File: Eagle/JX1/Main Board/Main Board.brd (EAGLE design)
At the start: 95.2 x 67.3 mm, 16 parts, among them U1 SN74HC595N, U2 SN74HC595N

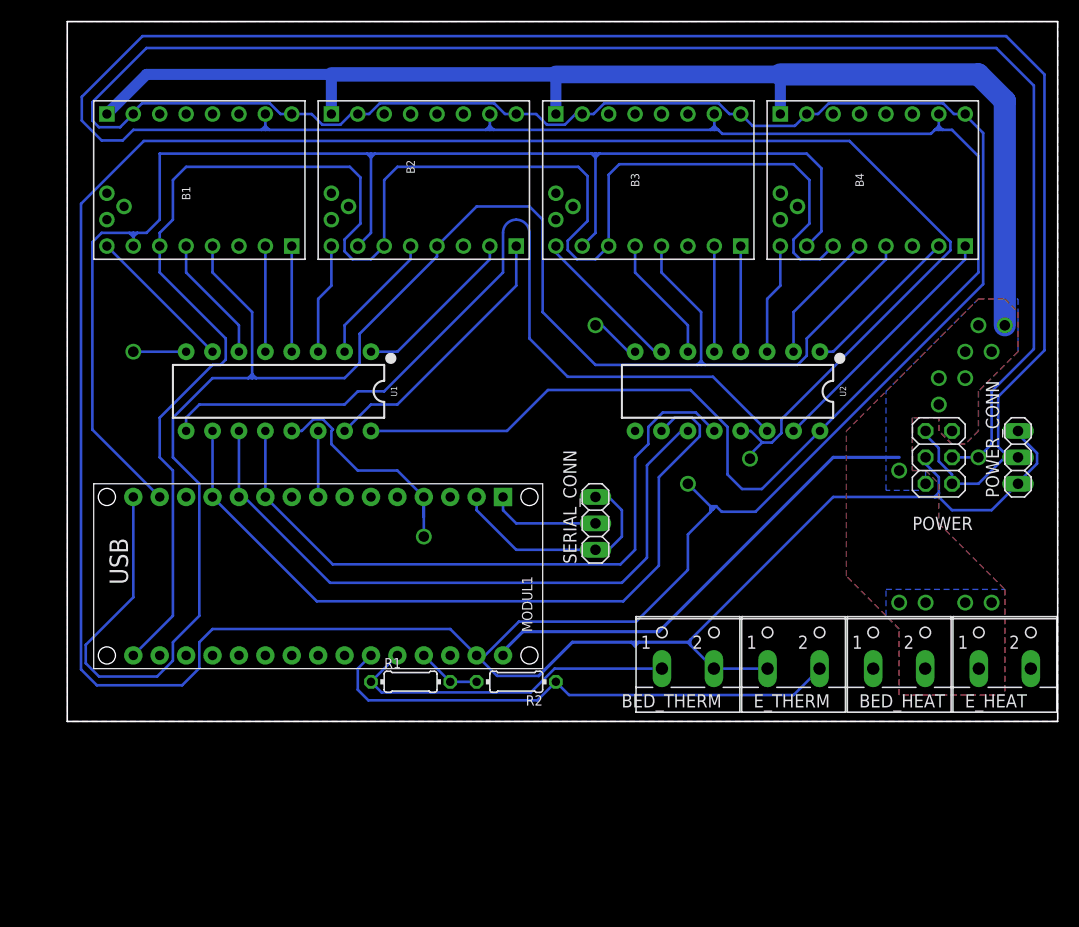
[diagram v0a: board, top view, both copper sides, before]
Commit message: Started added power mosfets for heaters
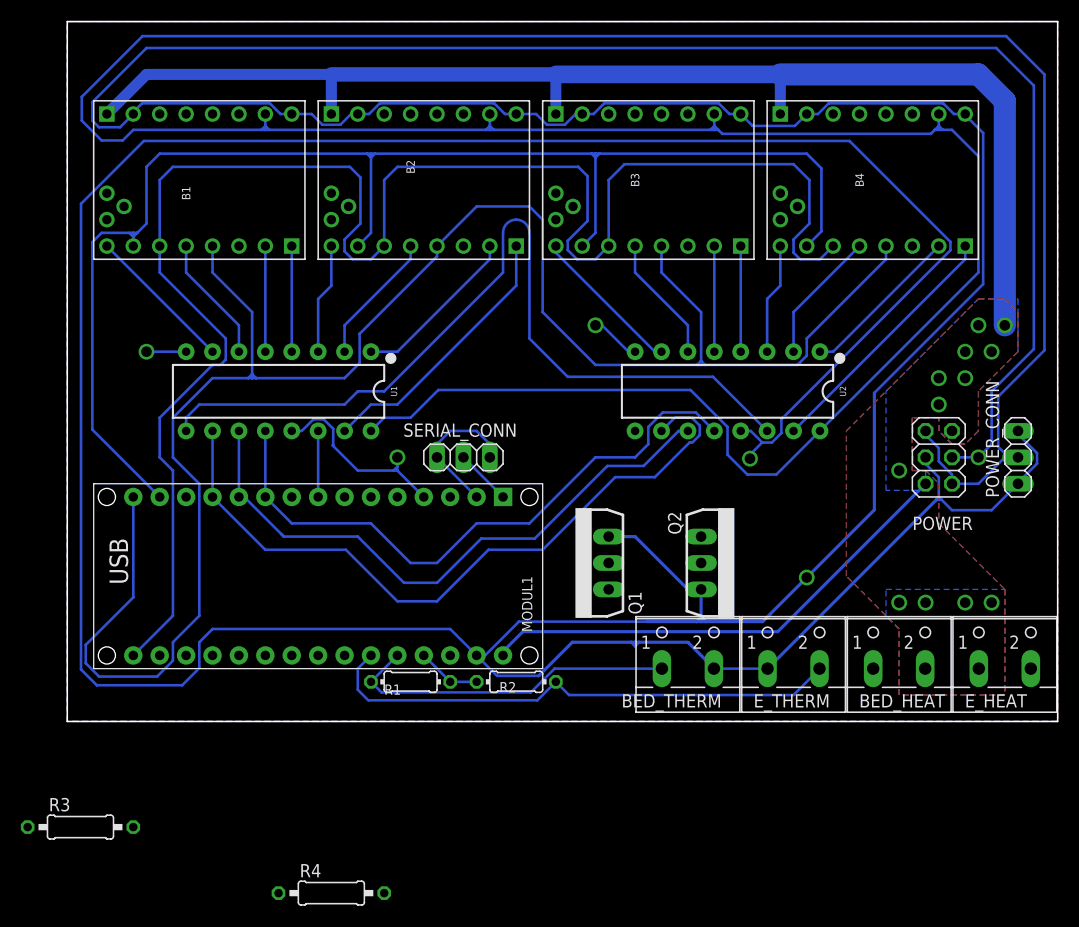
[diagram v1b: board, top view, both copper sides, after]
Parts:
- added Q1, Q2: IRF3704L-V, transistor-power:TO262-V
- added R3, R4: 1k, eagle-ltspice:0207/10
- moved SERIAL_CONN 14.2 mm to (38.1, 25.4), turned to 180 degrees
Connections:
- new net N$4: E_HEAT.2, Q1.2
- new net N$5: Q2.1, R3.2
- new net N$6: BED_HEAT.1, Q2.2
- new net N$7: Q1.1, R4.2
- new net N$8: R4.1
- new net N$9: R3.1
- net GND: now also Q1.3, Q2.3
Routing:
- net N$27: track 23.0 -> 14.1 mm
- net RCK: track 65.2 -> 59.9 mm
- net N$1: track 10.7 -> 5.39 mm
- net SSCK: track 64.2 -> 59.0 mm
- net SCL: track 74.5 -> 69.4 mm
- net GND: track 642.3 -> 645.7 mm
- net +5V: track 337.5 -> 335.2 mm
- net +12V: track 168.2 -> 169.7 mm
- net MOSI: track 137.4 -> 136.9 mm

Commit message: Finished thermal connections
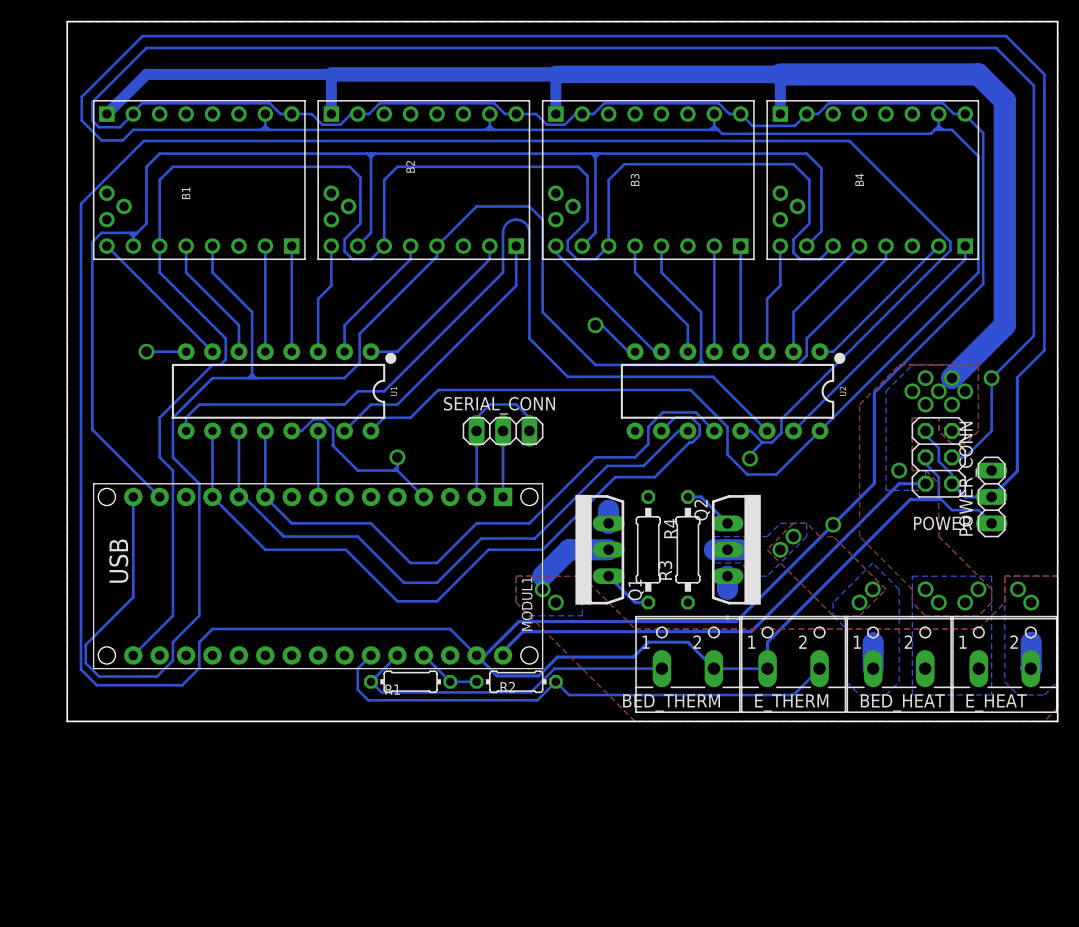
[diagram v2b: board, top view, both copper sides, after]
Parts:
- moved R3 64.2 mm to (59.7, 16.5), turned to 90 degrees
- moved R4 44.9 mm to (55.9, 16.5), turned to 270 degrees
- moved SERIAL_CONN 4.58 mm to (41.9, 27.9)
- moved POWER_CONN 4.58 mm to (88.9, 21.6)
- moved Q2 2.84 mm to (63.5, 16.5)
- moved Q1 1.27 mm to (52.1, 16.5)
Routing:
- net GND: track 645.7 -> 621.7 mm
- net N$4: track 0.00 -> 9.96 mm, vias 0 -> 4
- net +12V: track 169.7 -> 176.9 mm
- net N$6: track 0.00 -> 5.04 mm, vias 0 -> 4
- net N$7: track 0.00 -> 4.86 mm
- net N$5: track 0.00 -> 4.86 mm
- net N$1: track 5.39 -> 6.35 mm
- net N$27: track 14.1 -> 15.0 mm
- added copper zone on layer 1, net N$4
- added copper zone on layer 16, net N$4
- added copper zone on layer 1, net N$6
- added copper zone on layer 16, net N$6

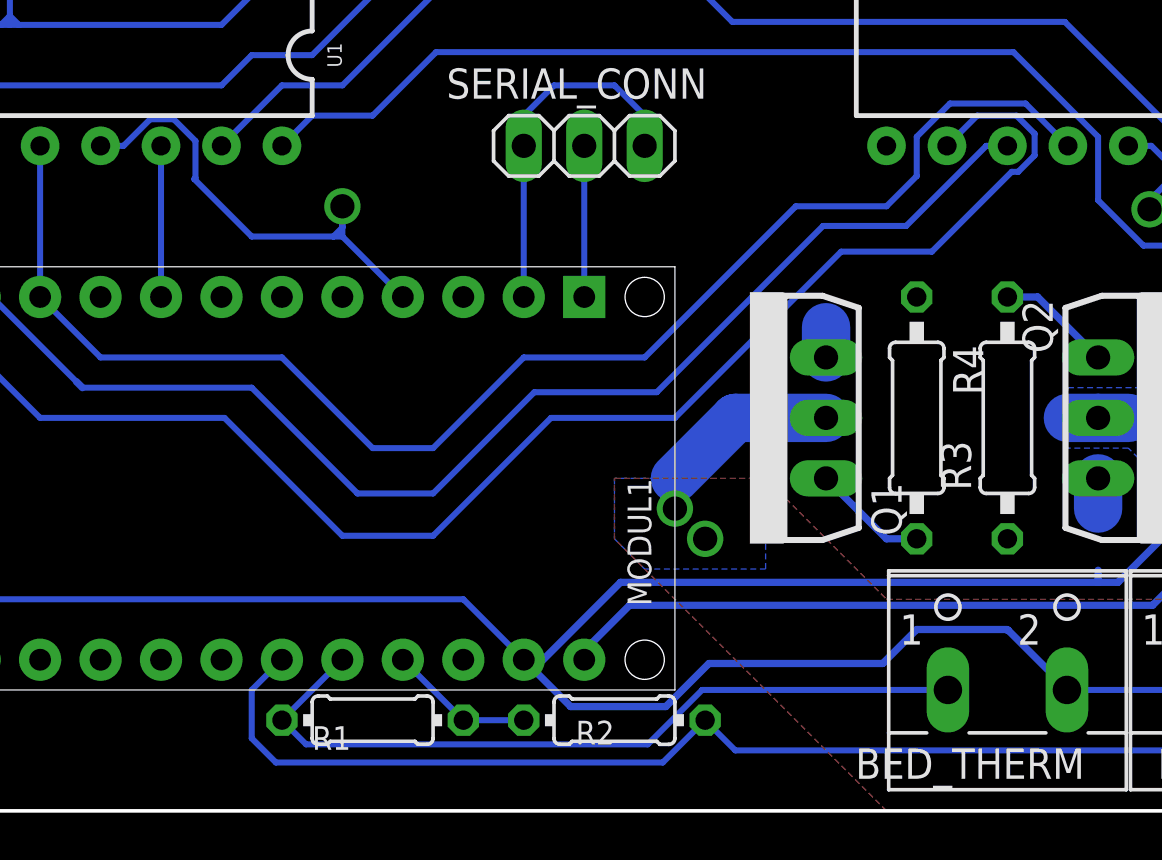
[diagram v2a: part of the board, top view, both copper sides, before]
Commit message: *Actually* finished thermal connections
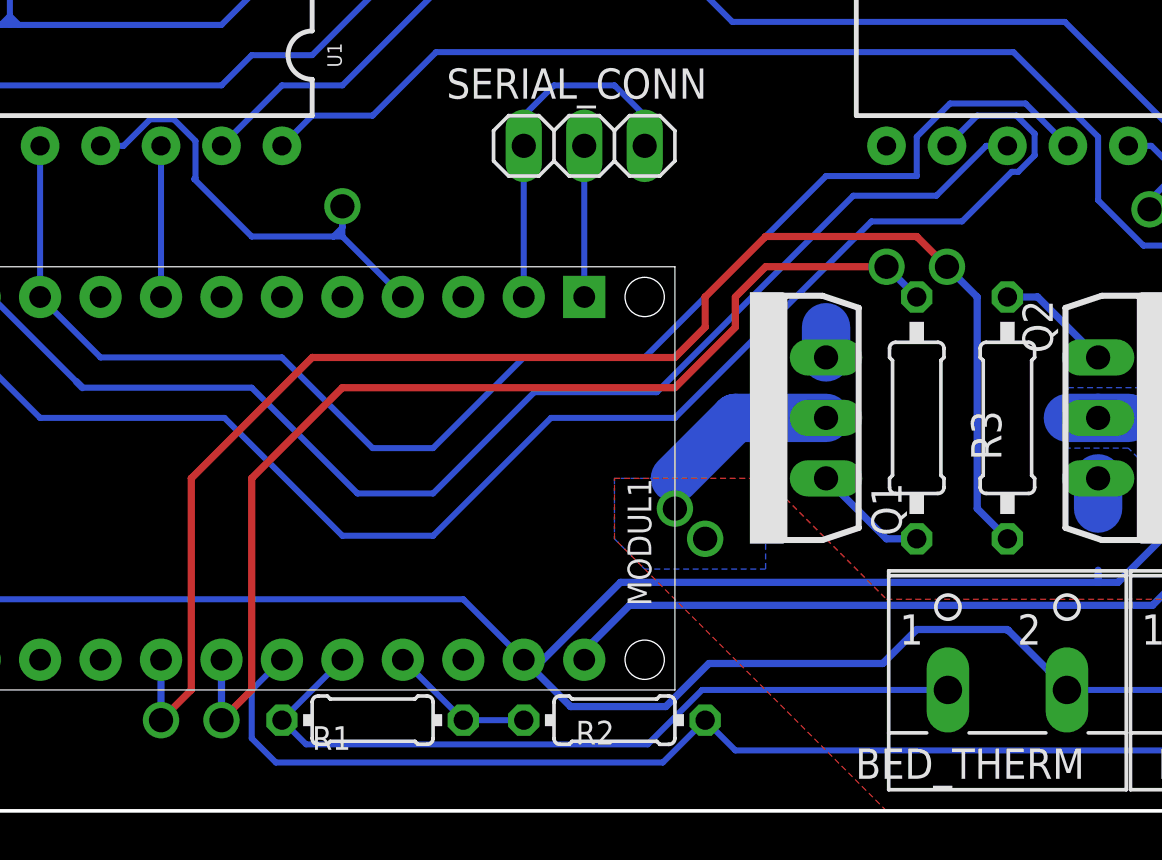
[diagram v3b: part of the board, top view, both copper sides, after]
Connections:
- removed net N$8: R4.1
- removed net N$9: R3.1
- new net BED_CON: MODUL1.J2.8, R3.1
- new net E_CON: MODUL1.J2.7, R4.1
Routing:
- net BED_CON: track 0.00 -> 62.9 mm, vias 0 -> 2
- net E_CON: track 0.00 -> 46.1 mm, vias 0 -> 2
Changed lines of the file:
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@@
 <drawing>
 <settings>
-<setting alwaysvectorfont="no"/>
+<setting alwaysvectorfont="yes"/>
 <setting verticaltext="up"/>
 </settings>
@@
 </layers>
 <board>
-<fusionsync huburn="a.cGVyc29uYWw6dWUyYjVlYjM4" projecturn="a.cGVyc29uYWw6dWUyYjVlYjM4IzIwMTgwMzE2MTIzMDY2Nzc2" f3durn="urn:adsk.wipprod:dm.lineage:FlkZ9POLT0O4GxRw0QSPzQ" pcbguid="07c534ba-3585-418c-91d1-b198318dc91a" lastpulledtime="" lastsyncedchangeguid="f7a266ec-bd81-444c-9fb9-cc551d47c649"/>
+<fusionsync huburn="a.cGVyc29uYWw6dWUyYjVlYjM4" projecturn="a.cGVyc29uYWw6dWUyYjVlYjM4IzIwMTgwMzE2MTIzMDY2Nzc2" f3durn="urn:adsk.wipprod:dm.lineage:FlkZ9POLT0O4GxRw0QSPzQ" pcbguid="07c534ba-3585-418c-91d1-b198318dc91a" lastpulledtime="" lastsyncedchangeguid="86579569-ff48-3005-335b-55d6a23f09b6"/>
 <plain>
 <text x="4.064" y="17.653" size="1.778" layer="112" rot="R270">USB</text>
@@
 </element>
 <element name="R3" library="eagle-ltspice" library_urn="urn:adsk.eagle:library:217" package="0207/10" package3d_urn="urn:adsk.eagle:package:13275/1" value="1k" x="59.69" y="16.51" smashed="yes" rot="R90">
-<attribute name="NAME" x="58.166" y="13.462" size="1.27" layer="25" ratio="10" rot="R90"/>
+<attribute name="NAME" x="59.436" y="14.732" size="1.27" layer="25" ratio="10" rot="R90"/>
 <attribute name="SPICEMODEL" value="NONE" x="59.69" y="16.51" size="1.778" layer="27" rot="R90" display="off"/>
 <attribute name="SPICEPREFIX" value="R" x="59.69" y="16.51" size="1.778" layer="27" rot="R90" display="off"/>
@@
 </element>
 <element name="R4" library="eagle-ltspice" library_urn="urn:adsk.eagle:library:217" package="0207/10" package3d_urn="urn:adsk.eagle:package:13275/1" value="1k" x="55.88" y="16.51" smashed="yes" rot="R270">
-<attribute name="NAME" x="57.404" y="19.558" size="1.27" layer="25" ratio="10" rot="R270"/>
 <attribute name="SPICEMODEL" value="NONE" x="55.88" y="16.51" size="1.778" layer="27" rot="R270" display="off"/>
 <attribute name="SPICEPREFIX" value="R" x="55.88" y="16.51" size="1.778" layer="27" rot="R270" display="off"/>
@@
 <wire x1="35.56" y1="11.557" x2="40.513" y2="16.51" width="0.254" layer="16"/>
 <wire x1="40.513" y1="16.51" x2="45.72" y2="16.51" width="0.254" layer="16"/>
-<wire x1="45.72" y1="16.51" x2="52.705" y2="23.495" width="0.254" layer="16"/>
-<wire x1="52.705" y1="23.495" x2="56.515" y2="23.495" width="0.254" layer="16"/>
+<wire x1="45.72" y1="16.51" x2="53.975" y2="24.765" width="0.254" layer="16"/>
+<wire x1="53.975" y1="24.765" x2="57.785" y2="24.765" width="0.254" layer="16"/>
 <wire x1="59.8678" y1="26.8478" x2="60.14240625" y2="26.8478" width="0.254" layer="16"/>
 <wire x1="60.14240625" y1="26.8478" x2="60.833" y2="27.53839375" width="0.254" layer="16"/>
 <wire x1="60.833" y1="27.53839375" x2="60.833" y2="28.448" width="0.254" layer="16"/>
-<wire x1="56.515" y1="23.495" x2="59.8678" y2="26.8478" width="0.254" layer="16"/>
+<wire x1="57.785" y1="24.765" x2="59.8678" y2="26.8478" width="0.254" layer="16"/>
 <wire x1="26.797" y1="16.51" x2="31.75" y2="11.557" width="0.254" layer="16"/>
 <wire x1="19.05" y1="16.51" x2="26.797" y2="16.51" width="0.254" layer="16"/>
@@
 <wire x1="19.05" y1="21.59" x2="19.05" y2="27.94" width="0.254" layer="16"/>
 <wire x1="19.05" y1="21.59" x2="21.59" y2="19.05" width="0.254" layer="16"/>
-<wire x1="54.61" y1="25.4" x2="55.88" y2="26.67" width="0.254" layer="16"/>
 <wire x1="57.277" y1="29.718" x2="55.88" y2="28.321" width="0.254" layer="16"/>
 <wire x1="62.23" y1="27.94" x2="60.452" y2="29.718" width="0.254" layer="16"/>
@@
 <wire x1="35.56" y1="15.24" x2="39.37" y2="19.05" width="0.254" layer="16"/>
 <wire x1="39.37" y1="19.05" x2="44.45" y2="19.05" width="0.254" layer="16"/>
-<wire x1="50.8" y1="25.4" x2="54.61" y2="25.4" width="0.254" layer="16"/>
-<wire x1="44.45" y1="19.05" x2="50.8" y2="25.4" width="0.254" layer="16"/>
+<wire x1="52.07" y1="26.67" x2="55.88" y2="26.67" width="0.254" layer="16"/>
+<wire x1="44.45" y1="19.05" x2="52.07" y2="26.67" width="0.254" layer="16"/>
 <wire x1="21.59" y1="19.05" x2="29.21" y2="19.05" width="0.254" layer="16"/>
 <wire x1="29.21" y1="19.05" x2="33.02" y2="15.24" width="0.254" layer="16"/>
@@
 <wire x1="32.385" y1="13.335" x2="35.56" y2="13.335" width="0.254" layer="16"/>
 <wire x1="59.69" y1="27.94" x2="58.801" y2="27.94" width="0.254" layer="16"/>
-<wire x1="55.4355" y1="24.5745" x2="58.801" y2="27.94" width="0.254" layer="16"/>
+<wire x1="56.7055" y1="25.8445" x2="58.801" y2="27.94" width="0.254" layer="16"/>
 <wire x1="35.56" y1="13.335" x2="39.8145" y2="17.5895" width="0.254" layer="16"/>
 <wire x1="39.8145" y1="17.5895" x2="44.958" y2="17.5895" width="0.254" layer="16"/>
-<wire x1="44.958" y1="17.5895" x2="51.943" y2="24.5745" width="0.254" layer="16"/>
-<wire x1="51.943" y1="24.5745" x2="55.4355" y2="24.5745" width="0.254" layer="16"/>
+<wire x1="44.958" y1="17.5895" x2="53.213" y2="25.8445" width="0.254" layer="16"/>
+<wire x1="53.213" y1="25.8445" x2="56.7055" y2="25.8445" width="0.254" layer="16"/>
 <wire x1="27.94" y1="17.78" x2="32.385" y2="13.335" width="0.254" layer="16"/>
 <wire x1="20.574" y1="18.034" x2="20.828" y2="17.78" width="0.3048" layer="16"/>
@@
 </polygon>
 </signal>
-<signal name="N$8">
+<signal name="BED_CON">
+<contactref element="R3" pad="1"/>
+<contactref element="MODUL1" pad="J2.8"/>
+<via x="57.15" y="22.86" extent="1-16" drill="1.02"/>
+<wire x1="59.69" y1="11.43" x2="58.42" y2="12.7" width="0.3048" layer="16"/>
+<wire x1="58.42" y1="12.7" x2="58.42" y2="21.59" width="0.3048" layer="16"/>
+<wire x1="58.42" y1="21.59" x2="57.15" y2="22.86" width="0.3048" layer="16"/>
+<wire x1="57.15" y1="22.86" x2="55.88" y2="24.13" width="0.3048" layer="1"/>
+<wire x1="55.88" y1="24.13" x2="49.53" y2="24.13" width="0.3048" layer="1"/>
+<wire x1="49.53" y1="24.13" x2="46.99" y2="21.59" width="0.3048" layer="1"/>
+<wire x1="46.99" y1="21.59" x2="46.99" y2="20.32" width="0.3048" layer="1"/>
+<wire x1="46.99" y1="20.32" x2="45.72" y2="19.05" width="0.3048" layer="1"/>
+<wire x1="45.72" y1="19.05" x2="30.48" y2="19.05" width="0.3048" layer="1"/>
+<wire x1="30.48" y1="19.05" x2="25.4" y2="13.97" width="0.3048" layer="1"/>
+<wire x1="25.4" y1="13.97" x2="25.4" y2="5.08" width="0.3048" layer="1"/>
+<via x="24.13" y="3.81" extent="1-16" drill="1.02"/>
+<wire x1="25.4" y1="5.08" x2="24.13" y2="3.81" width="0.3048" layer="1"/>
+<wire x1="24.13" y1="3.81" x2="24.13" y2="6.35" width="0.3048" layer="16"/>
+</signal>
+<signal name="E_CON">
 <contactref element="R4" pad="1"/>
-</signal>
-<signal name="N$9">
-<contactref element="R3" pad="1"/>
+<contactref element="MODUL1" pad="J2.7"/>
+<via x="26.67" y="3.81" extent="1-16" drill="1.02"/>
+<wire x1="26.67" y1="6.35" x2="26.67" y2="3.81" width="0.3048" layer="16"/>
+<wire x1="26.67" y1="3.81" x2="27.94" y2="5.08" width="0.3048" layer="1"/>
+<wire x1="27.94" y1="5.08" x2="27.94" y2="13.97" width="0.3048" layer="1"/>
+<wire x1="27.94" y1="13.97" x2="31.75" y2="17.78" width="0.3048" layer="1"/>
+<wire x1="31.75" y1="17.78" x2="45.72" y2="17.78" width="0.3048" layer="1"/>
+<wire x1="45.72" y1="17.78" x2="48.26" y2="20.32" width="0.3048" layer="1"/>
+<wire x1="48.26" y1="20.32" x2="48.26" y2="21.59" width="0.3048" layer="1"/>
+<wire x1="48.26" y1="21.59" x2="49.53" y2="22.86" width="0.3048" layer="1"/>
+<via x="54.61" y="22.86" extent="1-16" drill="1.02"/>
+<wire x1="49.53" y1="22.86" x2="54.61" y2="22.86" width="0.3048" layer="1"/>
+<wire x1="54.61" y1="22.86" x2="55.88" y2="21.59" width="0.3048" layer="16"/>
 </signal>
 </signals>
